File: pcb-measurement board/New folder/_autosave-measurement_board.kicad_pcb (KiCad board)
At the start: 4 copper layers, 60 x 45 mm, 92 parts, among them P1 HDR DUAL ROW, P2 CONN_02X15, P3 CONN_02X13, P4 CONN_02X05, P5 CONN_02X05, Q1 Si1101X, U1 NX3L4051, U10 TLV1G125, U11 NX3L4051, U12 MSP430G2955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

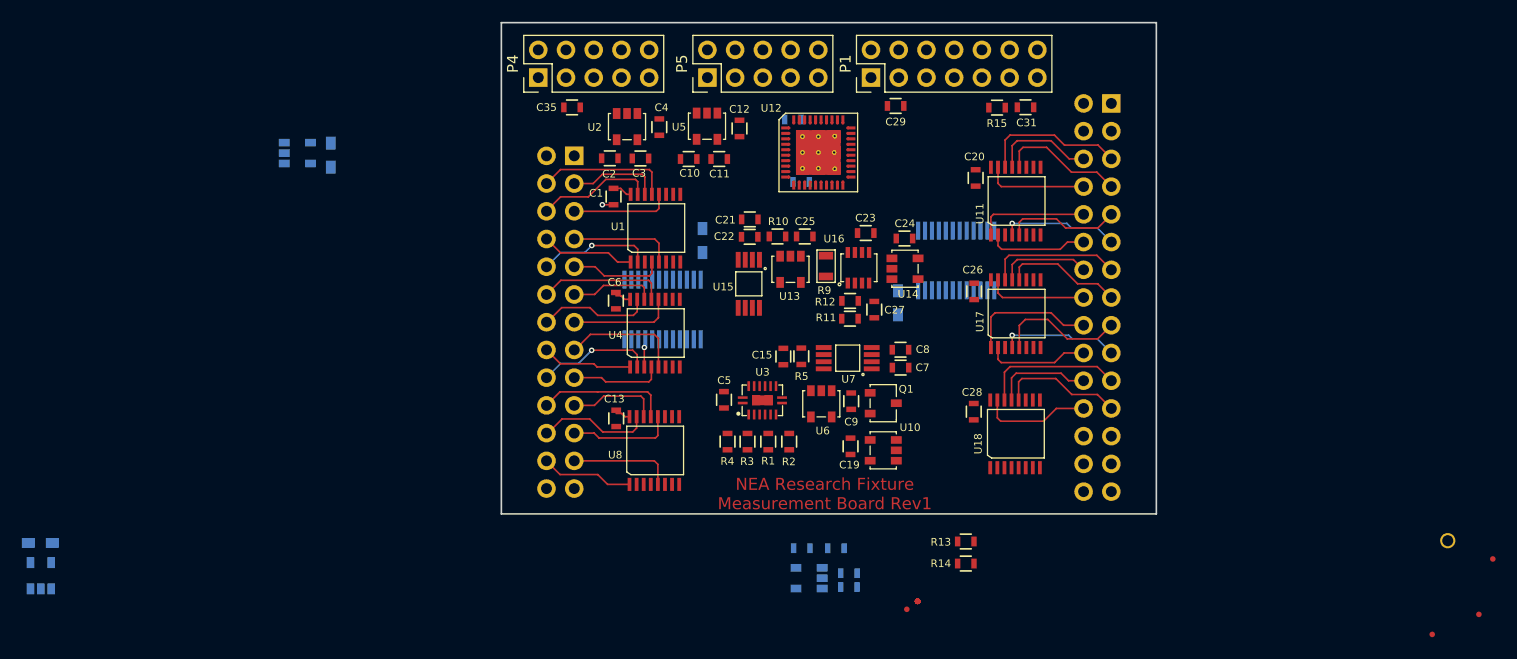
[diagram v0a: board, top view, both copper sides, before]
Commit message: -replaced all measurement board 0402 components with 0603 -adjusted placement and started routing on the layout
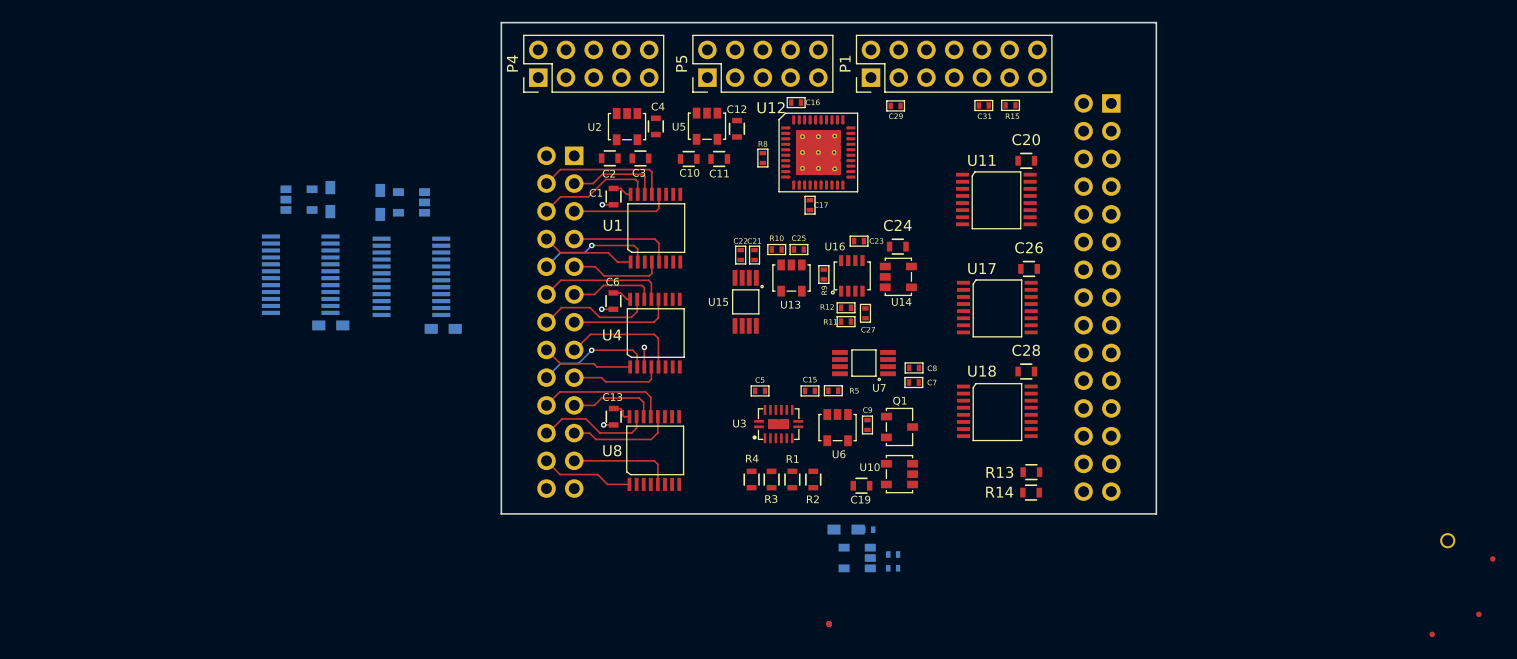
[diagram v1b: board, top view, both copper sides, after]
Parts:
- removed C35: 10uF, footprints_on_Cdrive:0603
- added R8: 47K, footprints_on_Cdrive:0402, F.Cu at (-6.05, -12.6)
- C14: value 1.1nF -> 1nF; footprint footprints_on_Cdrive:0603 -> footprints_on_Cdrive:0402
- C15, C21, C22, C23, C25, C27, C29, C31, C5, C7, C8, C9, R10, R11, R12, R15, R5, R6: footprint footprints_on_Cdrive:0603 -> footprints_on_Cdrive:0402
- C16, C17: footprint footprints_on_Cdrive:0603 -> footprints_on_Cdrive:0402; moved to F.Cu
- C18: footprint footprints_on_Cdrive:0603 -> Resistors_SMD:R_0603_HandSoldering
- R7: value 100k -> 100K; footprint footprints_on_Cdrive:0603 -> footprints_on_Cdrive:0402
- R9: value 10ohm 0.1% -> 10; footprint footprints_on_Cdrive:0805 -> footprints_on_Cdrive:0402
- moved U22 49.9 mm to (-37.0, -8.53), turned to 90 degrees
- moved U20 49.7 mm to (-41.0, 1.78), turned to 90 degrees
- moved C34 44.1 mm to (-41.1, -8.53), turned to 90 degrees
- moved C32 41.7 mm to (-35.3, 3.05), turned to 180 degrees
- moved U19 39.4 mm to (-51.1, 1.58), turned to 90 degrees
- moved C30 34.9 mm to (-45.6, 2.73), turned to 180 degrees
- moved R14 8.83 mm to (18.5, 18.0)
- moved R13 8.74 mm to (18.6, 16.2)
- moved TP10 8.39 mm to (0.00, 30.1)
- moved TP11 8.39 mm to (0.00, 30.1)
- moved TP12 8.39 mm to (0.00, 30.1)
- moved TP13 8.39 mm to (0.00, 30.1)
- moved TP14 8.39 mm to (0.00, 30.1)
- moved TP15 8.39 mm to (0.00, 30.1)
- moved TP4 8.39 mm to (0.00, 30.1)
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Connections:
- C4 pad 1: /5V -> /VIN
- R15 pad 1: /~RST -> /3V3
- R15 pad 2: /3V3 -> /~RST
- R6 pad 1: Net-(C14-Pad1) -> Net-(R6-Pad1)
- R6 pad 2: Net-(R6-Pad2) -> Net-(C14-Pad1)
- R7 pad 1: GND -> /~SELG
- R7 pad 2: /~SELG -> GND
- U16 pad 5: Net-(C23-Pad2) -> Net-(C23-Pad1)
- U16 pad 6: Net-(C23-Pad1) -> Net-(C23-Pad2)
- U2 pad 1: /5V -> /VIN
- U2 pad 3: /5V -> /VIN
- U9 pad 2: Net-(R6-Pad2) -> Net-(R6-Pad1)
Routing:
- net /M2: track 13.3 -> 0.00 mm
- net /U2: track 13.1 -> 0.00 mm
- net /Q2: track 12.3 -> 0.00 mm
- net /S2: track 11.9 -> 0.00 mm
- net /S1: track 11.9 -> 0.00 mm
- net /N2: track 11.5 -> 0.00 mm
- net /V2: track 11.4 -> 0.00 mm
- net /R2: track 11.0 -> 0.00 mm
- net /T2: track 10.9 -> 0.00 mm, vias 1 -> 0
- net /P2: track 10.9 -> 0.00 mm, vias 1 -> 0
- net /O2: track 10.6 -> 0.00 mm
- net /O1: track 10.2 -> 0.00 mm
- net /V1: track 10.1 -> 0.00 mm
- net /N1: track 9.44 -> 0.00 mm
- net /T1: track 9.42 -> 0.00 mm
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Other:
- board text removed: "NEA Research Fixture Measurement Board Rev1"
